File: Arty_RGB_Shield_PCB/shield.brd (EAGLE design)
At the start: 86.3 x 58.4 mm, 23 parts, among them IC1 SN74ALVC164245, IC2 SN74ALVC164245, IC3 TXS0104EPWR

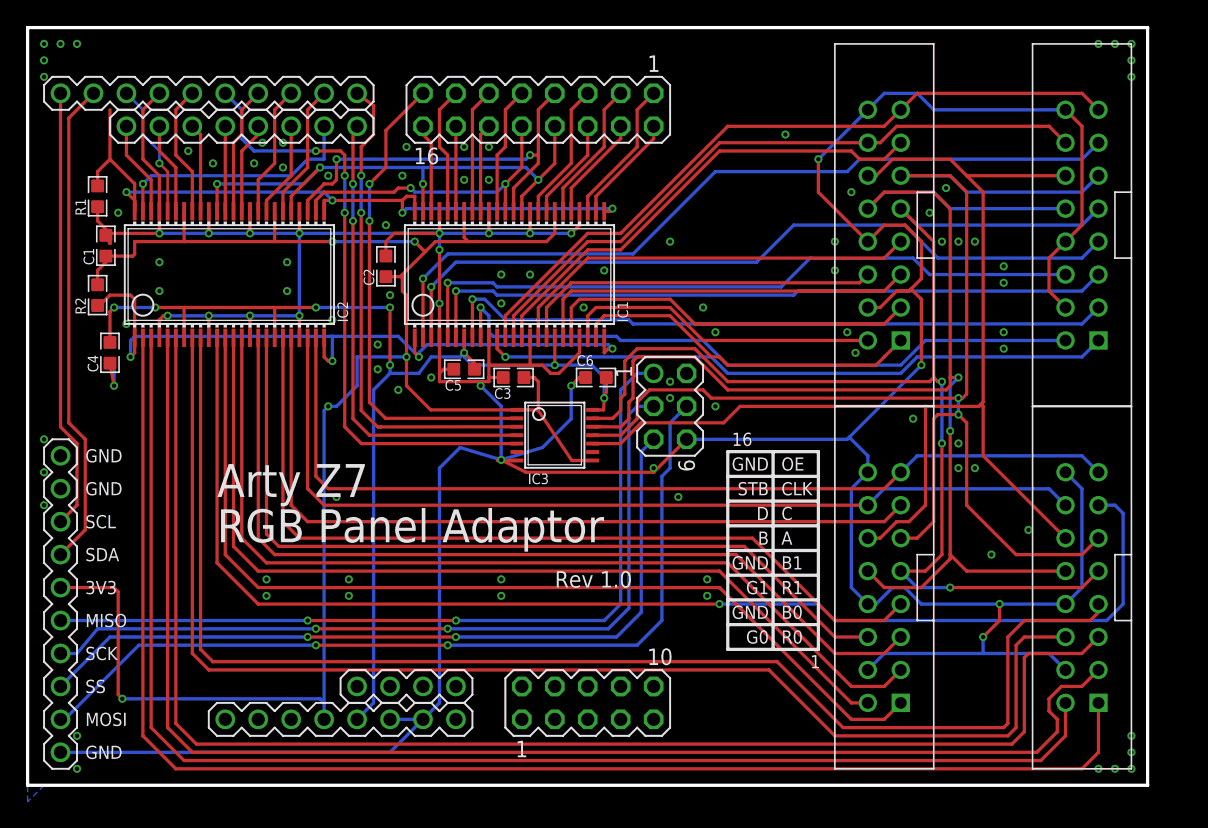
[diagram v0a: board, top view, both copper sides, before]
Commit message: add V2 board
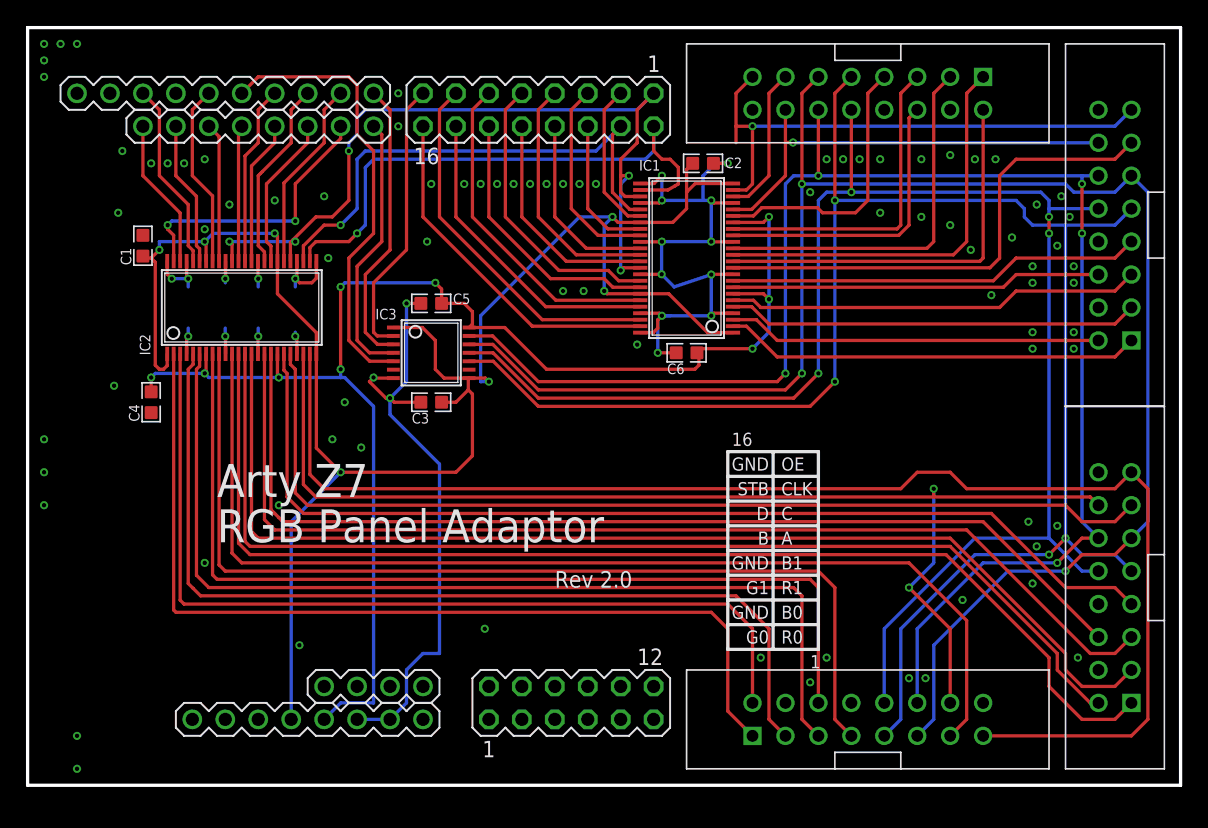
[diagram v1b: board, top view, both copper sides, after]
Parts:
- removed R1, R2: 10K, GadgetFactory:0603
- removed SV2: (no value), con-lstb:MA03-2
- removed U$11: PIN-1X10, alvie:PIN-1X10
- IC1, IC2: value SN74ALVC164245 -> SN74ALVC164245DGG; device alvie:SSOP48DL -> alvie:TSSOP48
- SV3: device con-lstb:MA05-2 -> con-lstb:MA06-2
- moved C2 25.7 mm to (52.1, 47.9), turned to 180 degrees
- moved IC1 14.0 mm to (50.8, 40.6), turned to 90 degrees
- moved IC3 11.4 mm to (31.1, 33.3)
- moved U$3 10.2 mm to (64.8, 53.3), turned to 180 degrees
- moved U$5 10.2 mm to (64.8, 5.08), turned to 0 degrees
- moved C6 7.24 mm to (50.8, 33.3)
- moved C3 6.63 mm to (31.1, 29.5)
- moved C5 5.68 mm to (31.1, 37.1)
- moved C4 4.96 mm to (9.53, 29.5)
- moved C1 2.86 mm to (8.89, 41.6)
- moved IC2 2.84 mm to (16.5, 36.8)
- moved SV4 2.54 mm to (26.7, 7.62)
- moved U$8 2.54 mm to (21.6, 5.08)
- moved U$4 2.54 mm to (83.8, 43.2)
- moved U$6 2.54 mm to (83.8, 15.2)
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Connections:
- removed net BUFF_DIR: IC1.1, IC1.24, IC2.1, IC2.24, R2.1
- removed net BUFF_OE: IC1.25, IC1.48, IC2.25, IC2.48, R1.1
- removed net IO0: IC1.27, SV1.1
- removed net IO26: IC1.26, SV1.2
- removed net IO27: IC1.29, SV1.4
- removed net MISO: SV2.1, U$11.5
- removed net MOSI: SV2.4, U$11.2
- removed net SCK: SV2.3, U$11.4
- removed net SCL: U$11.8, U$9.10
- removed net SDA: U$11.7, U$9.9
- removed net SS: SV2.5, U$11.3
- new net IO0/CLK: IC1.27, IC1.38, IC2.29, IC2.38, SV1.1
- new net IO26/OE: IC1.26, IC2.26, SV1.2
- new net IO27/STB: IC1.29, IC2.27, SV1.4
- net 12OE: now also IC1.23; no longer IC1.12
- net 12STB: now also IC1.20; no longer IC1.13
- net 1B0: now also IC1.14; no longer IC1.20
- net 1B1: now also IC1.19; no longer IC1.16
- net 1CLK: now also IC1.22; no longer IC1.14
- net 1G0: now also IC1.12; no longer IC1.22
- net 1G1: now also IC1.16; no longer IC1.17
- net 1R0: now also IC1.13; no longer IC1.23
- net 1R1: now also IC1.17; no longer IC1.19
- net 2B0: now also IC1.5; no longer IC1.8
- net 2B1: now also IC1.9; no longer IC1.3
- net 2CLK: now also IC1.11; no longer IC1.2
- net 2G0: now also IC1.3; no longer IC1.9
- net 2G1: now also IC1.8; no longer IC1.5
- net 2R0: now also IC1.2; no longer IC1.11
- net 3B0: now also IC2.5; no longer IC2.14
- net 3B1: now also IC2.9; no longer IC2.19
- net 3CLK: now also IC2.11; no longer IC2.20
- net 3G0: now also IC2.3; no longer IC2.13
- net 3G1: now also IC2.8; no longer IC2.17
- net 3R0: now also IC2.2; no longer IC2.12
- net 3R1: now also IC2.6; no longer IC2.16
- net 3V3: now also IC1.1, IC1.24, IC2.1, IC2.24; no longer R2.2, U$11.6
- net 4B0: now also IC2.14; no longer IC2.5
- net 4B1: now also IC2.19; no longer IC2.9
- net 4CLK: now also IC2.20; no longer IC2.11
- net 4G0: now also IC2.13; no longer IC2.3
- net 4G1: now also IC2.17; no longer IC2.8
- net 4R0: now also IC2.12; no longer IC2.2
- net 4R1: now also IC2.16; no longer IC2.6
- net A: now also IC3.10; no longer IC3.13
- net B: now also IC3.11; no longer IC3.12
- net C: now also IC3.12; no longer IC3.11
- net D: now also IC3.13; no longer IC3.10
- net GND: now also IC1.25, IC1.48, IC2.25, IC2.48; no longer R1.2, SV2.6, U$11.1, U$11.10, U$11.9
- net IO29: no longer IC1.47, IC2.29, IC2.38
- net IO3: no longer IC2.27
- net IO30: no longer IC2.26
- net IO31: now also IC1.41; no longer IC1.40
- net IO32: now also IC1.44; no longer IC1.43
- net IO33: now also IC1.47; no longer IC1.46
- net IO4: now also IC1.40; no longer IC1.38
- net IO5: now also IC1.43; no longer IC1.41
- net IO6: now also IC1.46; no longer IC1.44
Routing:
- net GND: track 369.3 -> 123.3 mm, vias 111 -> 106
- net MOSI: track 66.8 -> 0.00 mm, vias 2 -> 0
- net IO0/CLK: track 0.00 -> 64.5 mm, vias 0 -> 5
- net MISO: track 63.3 -> 0.00 mm, vias 2 -> 0
- net SCK: track 62.5 -> 0.00 mm, vias 2 -> 0
- net SS: track 60.9 -> 0.00 mm, vias 2 -> 0
- net BUFF_OE: track 56.0 -> 0.00 mm, vias 4 -> 0
- net BUFF_DIR: track 55.5 -> 0.00 mm, vias 4 -> 0
- net IO26/OE: track 0.00 -> 43.8 mm, vias 0 -> 1
- net IO27/STB: track 0.00 -> 39.7 mm, vias 0 -> 1
- net SDA: track 37.7 -> 0.00 mm
- net A: track 96.2 -> 133.6 mm, vias 3 -> 4
- net 34OE: track 73.0 -> 107.5 mm
- net SCL: track 34.1 -> 0.00 mm
- net C: track 102.7 -> 132.4 mm, vias 2 -> 3
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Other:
- board size 86.3 x 58.4 mm -> 88.9 x 58.4 mm
- board text added: "Rev 2.0"
- board text removed: "3V3"
- board text removed: "MISO"
- board text removed: "MOSI"
- board text removed: "Rev 1.0"
- board text removed: "SCK"
- board text removed: "SCL"
- board text removed: "SDA"
- board text removed: "SS"
